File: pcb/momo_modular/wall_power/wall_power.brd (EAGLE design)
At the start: 27.5 x 30.5 mm, 18 parts

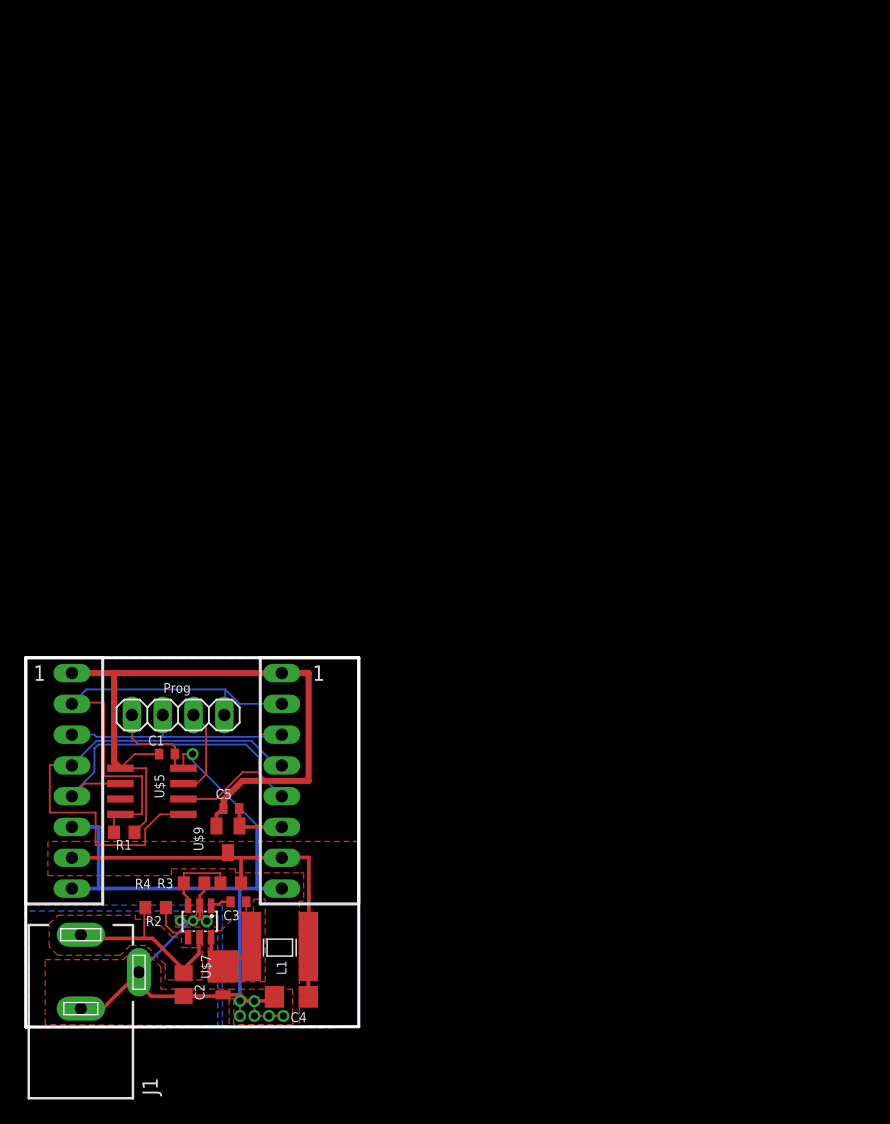
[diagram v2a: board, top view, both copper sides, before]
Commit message: Began combining wallpower and controller boards
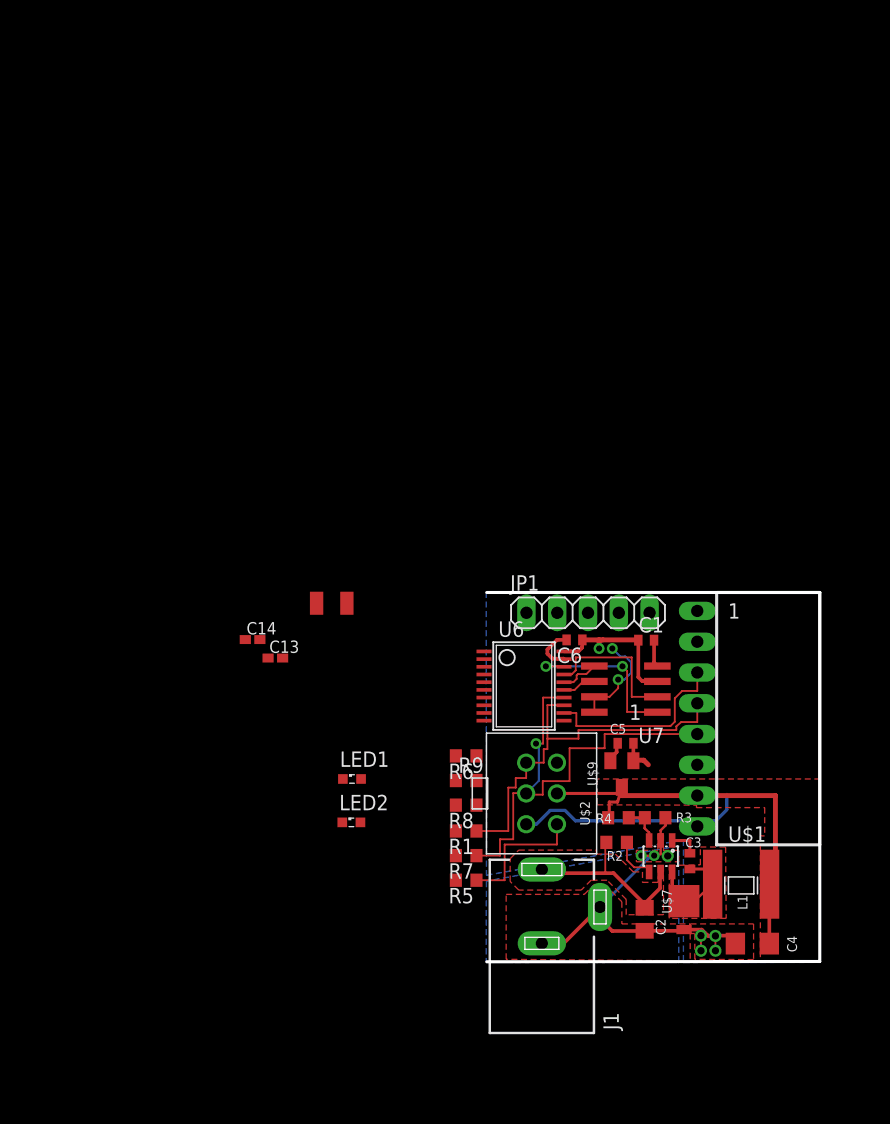
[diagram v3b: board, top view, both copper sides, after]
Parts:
- removed U$5: PIC12LF1822, components:SOIC8
- added C13, C14: 18 pF, rcl:C0402K
- added C6: 100 nF, rcl:C0402
- added LED1, LED2: (no value), led:SML0603
- added R5, R6, R7: 10K, rcl:R0603
- added R8, R9: 60R, rcl:R0603
- added U6: PIC24F16KA101-X_PSSOP, components:SSOP20
- added U7: FLASH8MSOP8, components:SOP08
- added XTAL1: 32.768khz, components:1206
- JP1: device pinhead:1X04 -> pinhead:1X05
- U$2: value MOMO-EDGE-8M -> MOMO-SENSOR-HEADER; device components:MOMO-EDGE-8M -> components:2X3-MOLEX-90130@1
- moved C1 40.6 mm to (51.2, 31.9)
- moved C2 38.4 mm to (51.1, 8.89)
- moved J1 38.4 mm to (42.6, 9.91)
- moved R2 38.4 mm to (48.8, 15.2)
- moved R4 38.4 mm to (51.9, 17.3)
- moved U$6 38.4 mm to (52.4, 14.1)
- moved U$7 38.4 mm to (54.3, 10.4)
- moved U$8 38.4 mm to (56.7, 11.8)
- moved C4 38.3 mm to (60.0, 6.88)
- moved U$2 37.5 mm to (41.3, 19.3), turned to 270 degrees
- moved C3 37.4 mm to (54.8, 13.7), turned to 270 degrees
- moved JP1 34.9 mm to (46.4, 34.2), turned to 0 degrees
- moved U$1 34.7 mm to (55.4, 24.2)
- moved C5 33.0 mm to (49.5, 23.4)
- moved U$9 33.0 mm to (49.2, 20.9)
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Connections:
- new net CS: U6.18, U7.1
- new net N$10: JP1.5, U6.5
- new net N$15: JP1.1, R6.1, U6.1
- new net N$24: C14.1, U6.10, XTAL1.P$2
- new net N$25: C13.1, U6.9, XTAL1.P$1
- new net N$5: LED2.A, R9.1
- new net N$7: LED1.A, R8.1
- new net N$9: JP1.4, U6.4
- new net SCLK: U6.15, U7.6
- new net SDI: U6.17, U7.2
- new net SDO: U6.16, U7.5
- net CLK: now also R5.1, U$2.3, U6.12; no longer JP1.3, U$2.CLK, U$5.6
- net DAT: now also R1.1, U$2.4, U6.13; no longer U$2.DAT, U$5.5
- net GND: now also C13.2, C14.2, C6.2, JP1.3, LED1.C, LED2.C, U$2.6, U6.19, U6.8, U7.4; no longer JP1.4, U$2.GND, U$2.PGND, U$5.8
- net IRQ: now also R7.1, U$2.5, U6.14; no longer U$2.ALRM, U$5.2
- net N$1: now also R9.2, U6.2; no longer JP1.1, R1.2, U$1.NV, U$2.NC, U$5.4
- net N$8: now also R8.2, U6.3; no longer JP1.2, U$5.7
- net V+: now also U$2.2; no longer U$2.V4
- net VCCINT: now also C6.1, R1.2, R5.2, R6.2, R7.2, U$2.1, U6.20, U7.3, U7.7, U7.8; no longer R1.1, U$2.V28, U$5.1
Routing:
- net GND: track 103.2 -> 62.6 mm, vias 10 -> 7
- net N$1: track 39.4 -> 0.00 mm
- net VCCINT: track 58.3 -> 22.7 mm, vias 0 -> 3
- net CS: track 0.00 -> 14.3 mm, vias 0 -> 2
- net IRQ: track 27.3 -> 39.5 mm, vias 0 -> 1
- net SDI: track 0.00 -> 12.2 mm
- net DAT: track 40.3 -> 32.7 mm
- net N$8: track 7.52 -> 0.00 mm
- net CLK: track 31.4 -> 27.2 mm
- net N$6: track 6.68 -> 3.36 mm
- net SDO: track 0.00 -> 3.24 mm
- net SCLK: track 0.00 -> 2.81 mm
- net N$2: track 9.79 -> 12.0 mm
- net V+: track 33.9 -> 34.8 mm
- net N$4: track 1.74 -> 2.52 mm
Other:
- board text removed: "Prog"

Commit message: Finalized the following boards for fabrication/assembly: Sensor Dev Board GSM Module Combined Wallpower and Controller Boards
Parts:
- removed C13, C14: 18 pF, rcl:C0402K
- removed U$2: MOMO-SENSOR-HEADER, components:2X3-MOLEX-90130@1
- added C7, C8: 18 pF, rcl:C0402K
- added JP3: MOMO-SENSOR-HEADER, components:2X3-MOLEX-90130
- D1: value DIODE_SS2P3 -> DIODE_SS2P3SS2P3
- moved LED1 14.9 mm to (37.3, 9.78), turned to 180 degrees
- moved XTAL1 13.8 mm to (35.4, 27.1), turned to 270 degrees
- moved LED2 13.3 mm to (37.3, 8.69), turned to 180 degrees
- moved C1 0.56 mm to (51.8, 32.0), turned to 180 degrees
- moved R8 0.08 mm to (36.3, 18.2)
- moved R9 0.05 mm to (36.3, 20.3), turned to 180 degrees
- turned C6 to 0 degrees
- renumbered J1 to JP4, U$1 to JP2, U$6 to U1, U$7 to D1, U$8 to L1, U$9 to U2, U6 to U3, U7 to U4
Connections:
- net CLK: now also JP3.3; no longer U$2.3
- net DAT: now also JP3.4; no longer U$2.4
- net GND: now also C7.2, C8.2, JP3.6, R8.1, R9.1; no longer C13.2, C14.2, LED1.C, LED2.C, U$2.6
- net IRQ: now also JP3.5; no longer U$2.5
- net N$1: now also LED2.A; no longer R9.2
- net N$24: now also C8.1; no longer C14.1
- net N$25: now also C7.1; no longer C13.1
- net N$5: now also LED2.C, R9.2; no longer LED2.A, R9.1
- net N$7: now also LED1.C, R8.2; no longer LED1.A, R8.1
- net N$8: now also LED1.A; no longer R8.2
- net V+: now also JP3.2; no longer U$2.2
- net VCCINT: now also JP1.2, JP3.1; no longer U$2.1
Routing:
- net VCCINT: track 22.7 -> 100.2 mm, vias 3 -> 6
- net GND: track 62.6 -> 129.5 mm, vias 7 -> 10
- net N$1: track 0.00 -> 32.1 mm
- net CLK: track 27.2 -> 58.4 mm
- net N$8: track 0.00 -> 29.9 mm
- net N$10: track 0.00 -> 21.6 mm, vias 0 -> 1
- net N$9: track 0.00 -> 20.4 mm, vias 0 -> 1
- net N$15: track 0.00 -> 19.7 mm
- net N$5: track 0.00 -> 16.6 mm
- net N$7: track 0.00 -> 12.7 mm
- net N$25: track 0.00 -> 4.82 mm
- net N$24: track 0.00 -> 4.59 mm
- added copper zone on layer 16, net VCCINT
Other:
- board size 27.5 x 30.5 mm -> 34.1 x 33 mm
- board text added: "MoMo Dev Controller"
